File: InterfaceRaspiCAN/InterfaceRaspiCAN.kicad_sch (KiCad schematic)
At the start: 30 parts, among them J1 Raspberry_Pi_2_3, J10 Conn_02x01, J11 Conn_02x01, J12 Conn_02x01, J13 Conn_01x02, J14 Conn_01x02, J15 Conn_01x02, J16 Conn_01x02, J2 CAN1, J3 CAN2, J4 I2C1_5, J5 I2C2_5, U1 MCP2517FD-xSL, U2 MCP2558FD-xSN, U3 PCF8574A, U4 PESD1CAN, Y2 40MHz

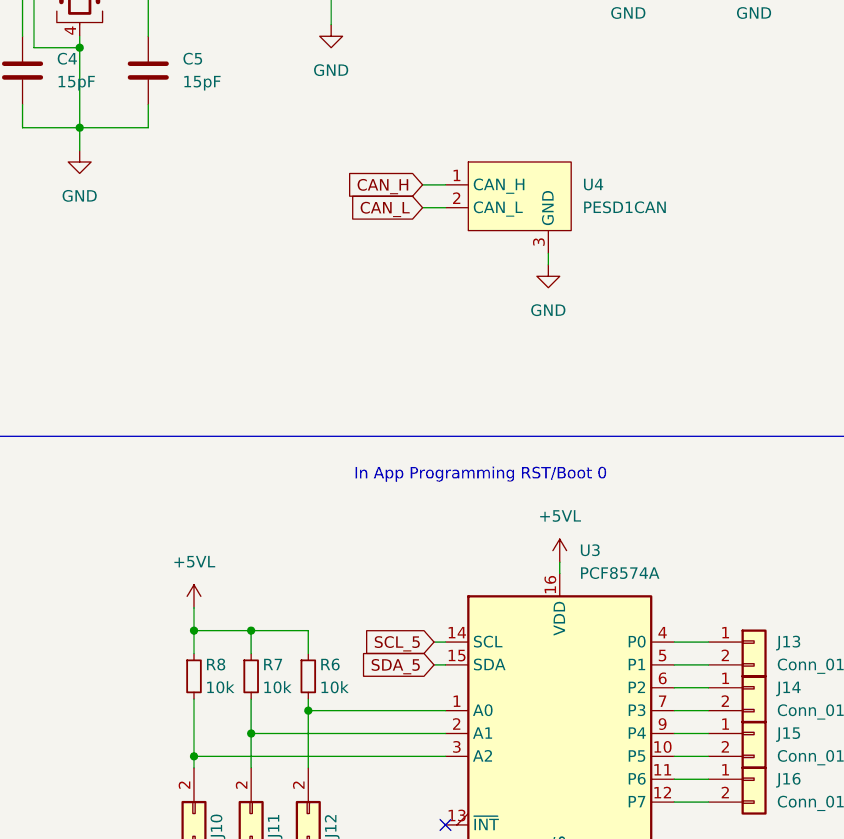
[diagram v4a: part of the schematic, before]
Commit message: In app programming on 3.3V
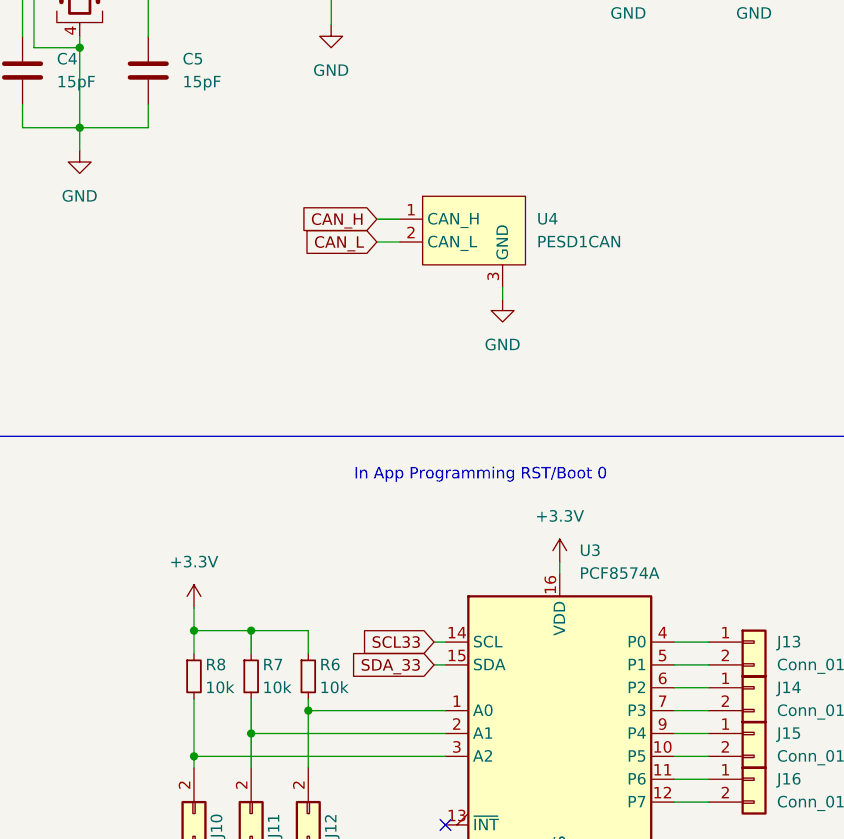
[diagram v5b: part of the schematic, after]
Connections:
- net +3.3V: now also R6.1, R7.1, R8.1, U3.16 (VDD)
- net +5VL: no longer R6.1, R7.1, R8.1, U3.16 (VDD)
- net SCL33: now also U3.14 (SCL)
- net SCL_5: no longer U3.14 (SCL)
- net SDA_33: now also U3.15 (SDA)
- net SDA_5: no longer U3.15 (SDA)
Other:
- moved on the sheet: U4
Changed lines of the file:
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@@
     (stroke (width 0) (type default))
   )
-  (wire (pts (xy 152.4 76.2) (xy 154.94 76.2))
+  (wire (pts (xy 147.32 80.01) (xy 149.86 80.01))
     (stroke (width 0) (type default))
   )
@@
     (stroke (width 0) (type default))
   )
-  (wire (pts (xy 166.37 83.82) (xy 166.37 85.09))
+  (wire (pts (xy 161.29 87.63) (xy 161.29 88.9))
     (stroke (width 0) (type default))
   )
@@
     (stroke (width 0) (type default))
   )
-  (wire (pts (xy 152.4 78.74) (xy 154.94 78.74))
+  (wire (pts (xy 147.32 82.55) (xy 149.86 82.55))
     (stroke (width 0) (type default))
   )
@@
     )
   )
-  (global_label "CAN_L" (shape input) (at 152.4 78.74 180) (fields_autoplaced)
-    (effects (font (size 1.27 1.27)) (justify right))
-    (property "Intersheetrefs" "${INTERSHEET_REFS}" (at 143.73 78.74 0)
+  (global_label "SCL33" (shape input) (at 153.67 127 180) (fields_autoplaced)
+    (effects (font (size 1.27 1.27)) (justify right))
+    (property "Intersheetrefs" "${INTERSHEET_REFS}" (at 144.7582 127 0)
+      (effects (font (size 1.27 1.27)) (justify right) hide)
+    )
+  )
+  (global_label "CAN_L" (shape input) (at 147.32 82.55 180) (fields_autoplaced)
+    (effects (font (size 1.27 1.27)) (justify right))
+    (property "Intersheetrefs" "${INTERSHEET_REFS}" (at 138.65 82.55 0)
       (effects (font (size 1.27 1.27)) (justify right) hide)
     )
@@
     )
   )
-  (global_label "SCL_5" (shape input) (at 153.67 127 180) (fields_autoplaced)
-    (effects (font (size 1.27 1.27)) (justify right))
-    (property "Intersheetrefs" "${INTERSHEET_REFS}" (at 145.0001 127 0)
-      (effects (font (size 1.27 1.27)) (justify right) hide)
-    )
-  )
   (global_label "SPI_MISO" (shape input) (at 80.01 114.3 0) (fields_autoplaced)
     (effects (font (size 1.27 1.27)) (justify left))
@@
     )
   )
-  (global_label "CAN_H" (shape input) (at 152.4 76.2 180) (fields_autoplaced)
-    (effects (font (size 1.27 1.27)) (justify right))
-    (property "Intersheetrefs" "${INTERSHEET_REFS}" (at 143.4276 76.2 0)
+  (global_label "CAN_H" (shape input) (at 147.32 80.01 180) (fields_autoplaced)
+    (effects (font (size 1.27 1.27)) (justify right))
+    (property "Intersheetrefs" "${INTERSHEET_REFS}" (at 138.3476 80.01 0)
       (effects (font (size 1.27 1.27)) (justify right) hide)
     )
@@
     (effects (font (size 1.27 1.27)) (justify right))
     (property "Intersheetrefs" "${INTERSHEET_REFS}" (at 169.7953 36.83 0)
+      (effects (font (size 1.27 1.27)) (justify right) hide)
+    )
+  )
+  (global_label "SDA_33" (shape input) (at 153.67 129.54 180) (fields_autoplaced)
+    (effects (font (size 1.27 1.27)) (justify right))
+    (property "Intersheetrefs" "${INTERSHEET_REFS}" (at 143.7301 129.54 0)
       (effects (font (size 1.27 1.27)) (justify right) hide)
     )
@@
     )
   )
-  (global_label "SDA_5" (shape input) (at 153.67 129.54 180) (fields_autoplaced)
-    (effects (font (size 1.27 1.27)) (justify right))
-    (property "Intersheetrefs" "${INTERSHEET_REFS}" (at 144.9396 129.54 0)
-      (effects (font (size 1.27 1.27)) (justify right) hide)
-    )
-  )
   (global_label "TX" (shape input) (at 175.26 34.29 180) (fields_autoplaced)
     (effects (font (size 1.27 1.27)) (justify right))
@@
     )
   )
-  (symbol (lib_id "ARIG:PESD1CAN") (at 157.48 73.66 0) (unit 1)
-    (in_bom yes) (on_board yes) (dnp no) (fields_autoplaced)
-    (property "Reference" "U4" (at 170.18 76.2 0)
-      (effects (font (size 1.27 1.27)) (justify left))
-    )
-    (property "Value" "PESD1CAN" (at 170.18 78.74 0)
-      (effects (font (size 1.27 1.27)) (justify left))
-    )
-    (property "Footprint" "Package_TO_SOT_SMD:SOT-23" (at 184.15 80.01 0)
-      (effects (font (size 1.27 1.27)) hide)
-    )
-    (property "Datasheet" "https://assets.nexperia.com/documents/data-sheet/PESD1CAN.pdf" (at 203.2 76.2 0)
+  (symbol (lib_id "ARIG:PESD1CAN") (at 152.4 77.47 0) (unit 1)
+    (in_bom yes) (on_board yes) (dnp no) (fields_autoplaced)
+    (property "Reference" "U4" (at 165.1 80.01 0)
+      (effects (font (size 1.27 1.27)) (justify left))
+    )
+    (property "Value" "PESD1CAN" (at 165.1 82.55 0)
+      (effects (font (size 1.27 1.27)) (justify left))
+    )
+    (property "Footprint" "Package_TO_SOT_SMD:SOT-23" (at 179.07 83.82 0)
+      (effects (font (size 1.27 1.27)) hide)
+    )
+    (property "Datasheet" "https://assets.nexperia.com/documents/data-sheet/PESD1CAN.pdf" (at 198.12 80.01 0)
       (effects (font (size 1.27 1.27)) hide)
     )
@@
     )
   )
-  (symbol (lib_id "power:+5VL") (at 167.64 118.11 0) (unit 1)
-    (in_bom yes) (on_board yes) (dnp no) (fields_autoplaced)
-    (property "Reference" "#PWR024" (at 167.64 121.92 0)
-      (effects (font (size 1.27 1.27)) hide)
-    )
-    (property "Value" "+5VL" (at 167.64 113.03 0)
-      (effects (font (size 1.27 1.27)))
-    )
-    (property "Footprint" "" (at 167.64 118.11 0)
-      (effects (font (size 1.27 1.27)) hide)
-    )
-    (property "Datasheet" "" (at 167.64 118.11 0)
+  (symbol (lib_id "power:+3.3V") (at 127 123.19 0) (unit 1)
+    (in_bom yes) (on_board yes) (dnp no) (fields_autoplaced)
+    (property "Reference" "#PWR024" (at 127 127 0)
+      (effects (font (size 1.27 1.27)) hide)
+    )
+    (property "Value" "+3.3V" (at 127 118.11 0)
+      (effects (font (size 1.27 1.27)))
+    )
+    (property "Footprint" "" (at 127 123.19 0)
+      (effects (font (size 1.27 1.27)) hide)
+    )
+    (property "Datasheet" "" (at 127 123.19 0)
       (effects (font (size 1.27 1.27)) hide)
     )
@@
     )
   )
+  (symbol (lib_id "power:+3.3V") (at 167.64 118.11 0) (unit 1)
+    (in_bom yes) (on_board yes) (dnp no) (fields_autoplaced)
+    (property "Reference" "#PWR025" (at 167.64 121.92 0)
+      (effects (font (size 1.27 1.27)) hide)
+    )
+    (property "Value" "+3.3V" (at 167.64 113.03 0)
+      (effects (font (size 1.27 1.27)))
+    )
+    (property "Footprint" "" (at 167.64 118.11 0)
+      (effects (font (size 1.27 1.27)) hide)
+    )
+    (property "Datasheet" "" (at 167.64 118.11 0)
+      (effects (font (size 1.27 1.27)) hide)
+    )
+    (pin "1")
+    (instances
+      (project "InterfaceRaspiCAN"
+        (path "/466ed181-1b10-43ca-b8d2-18d3e4c6e8d6"
+          (reference "#PWR025") (unit 1)
+        )
+      )
+    )
+  )
   (symbol (lib_id "Device:C") (at 83.82 31.75 0) (unit 1)
     (in_bom yes) (on_board yes) (dnp no)
@@
         (path "/466ed181-1b10-43ca-b8d2-18d3e4c6e8d6"
           (reference "J2") (unit 1)
-        )
-      )
-    )
-  )
-  (symbol (lib_id "power:+5VL") (at 127 123.19 0) (unit 1)
-    (in_bom yes) (on_board yes) (dnp no) (fields_autoplaced)
-    (property "Reference" "#PWR029" (at 127 127 0)
-      (effects (font (size 1.27 1.27)) hide)
-    )
-    (property "Value" "+5VL" (at 127 118.11 0)
-      (effects (font (size 1.27 1.27)))
-    )
-    (property "Footprint" "" (at 127 123.19 0)
-      (effects (font (size 1.27 1.27)) hide)
-    )
-    (property "Datasheet" "" (at 127 123.19 0)
-      (effects (font (size 1.27 1.27)) hide)
-    )
-    (pin "1")
-    (instances
-      (project "InterfaceRaspiCAN"
-        (path "/466ed181-1b10-43ca-b8d2-18d3e4c6e8d6"
-          (reference "#PWR029") (unit 1)
         )
       )
@@
     )
   )
-  (symbol (lib_id "power:GND") (at 166.37 85.09 0) (unit 1)
-    (in_bom yes) (on_board yes) (dnp no) (fields_autoplaced)
-    (property "Reference" "#PWR030" (at 166.37 91.44 0)
-      (effects (font (size 1.27 1.27)) hide)
-    )
-    (property "Value" "GND" (at 166.37 90.17 0)
-      (effects (font (size 1.27 1.27)))
-    )
-    (property "Footprint" "" (at 166.37 85.09 0)
-      (effects (font (size 1.27 1.27)) hide)
-    )
-    (property "Datasheet" "" (at 166.37 85.09 0)
-      (effects (font (size 1.27 1.27)) hide)
-    )
+  (symbol (lib_id "power:GND") (at 161.29 88.9 0) (unit 1)
+    (in_bom yes) (on_board yes) (dnp no) (fields_autoplaced)
+    (property "Reference" "#PWR030" (at 161.29 95.25 0)
+      (effects (font (size 1.27 1.27)) hide)
+    )
+    (property "Value" "GND" (at 161.29 93.98 0)
+      (effects (font (size 1.27 1.27)))
+    )
+    (property "Footprint" "" (at 161.29 88.9 0)
+      (effects (font (size 1.27 1.27)) hide)
+    )
+    (property "Datasheet" "" (at 161.29 88.9 0)
+      (effects (font (size 1.27 1.27)) hide)
+    )

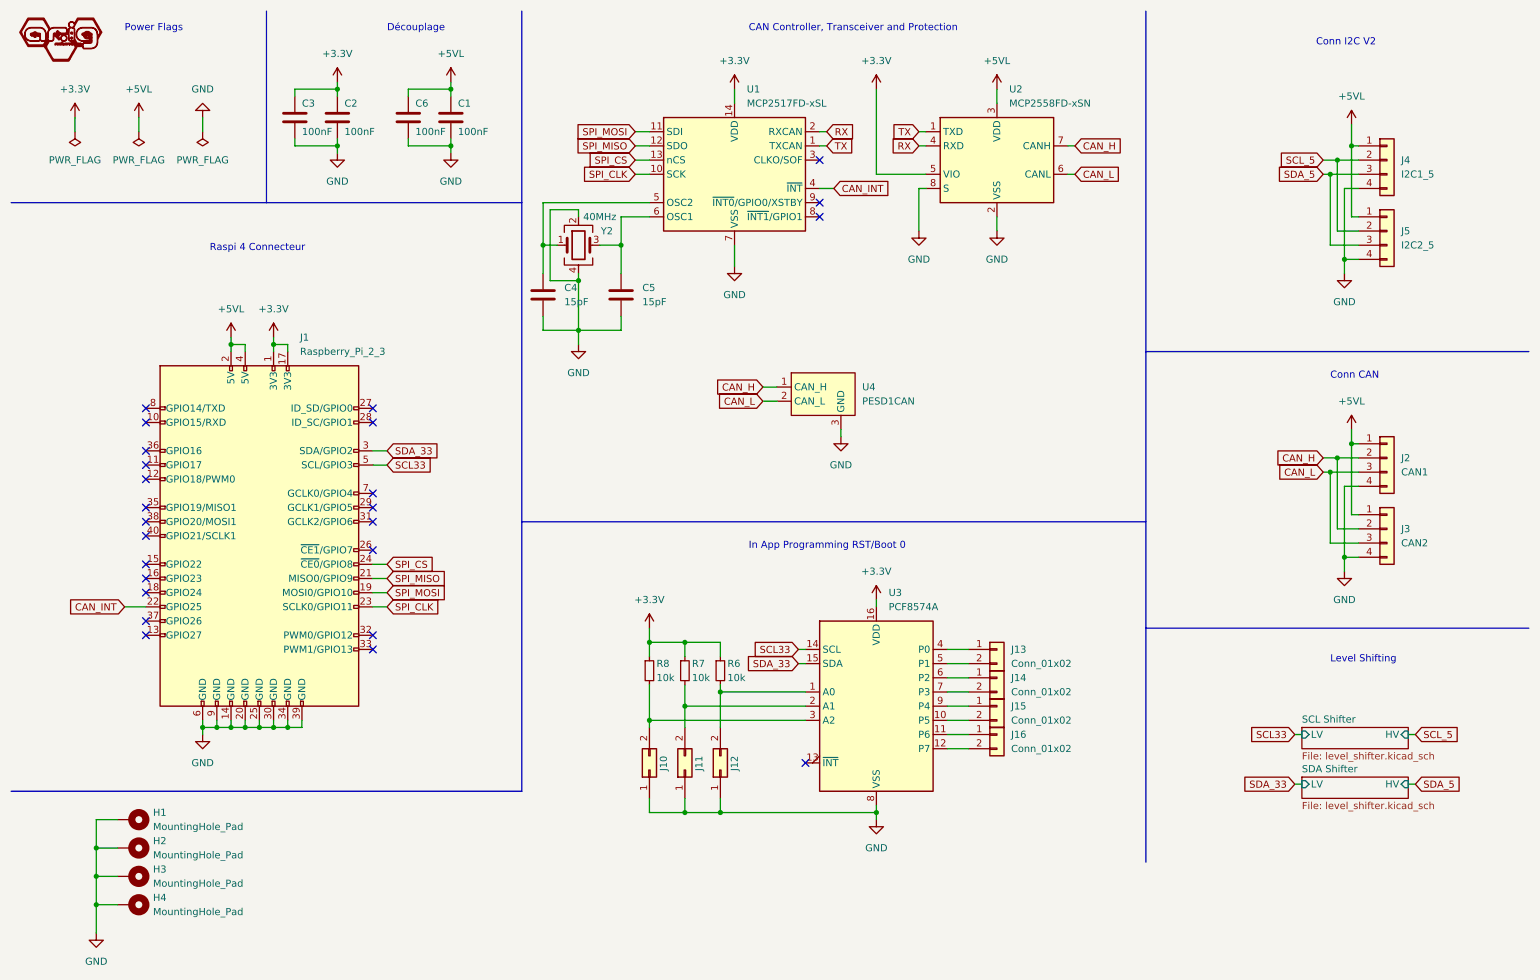
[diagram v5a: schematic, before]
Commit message: Fix CAN connections to improve routing on InterfaceRaspi
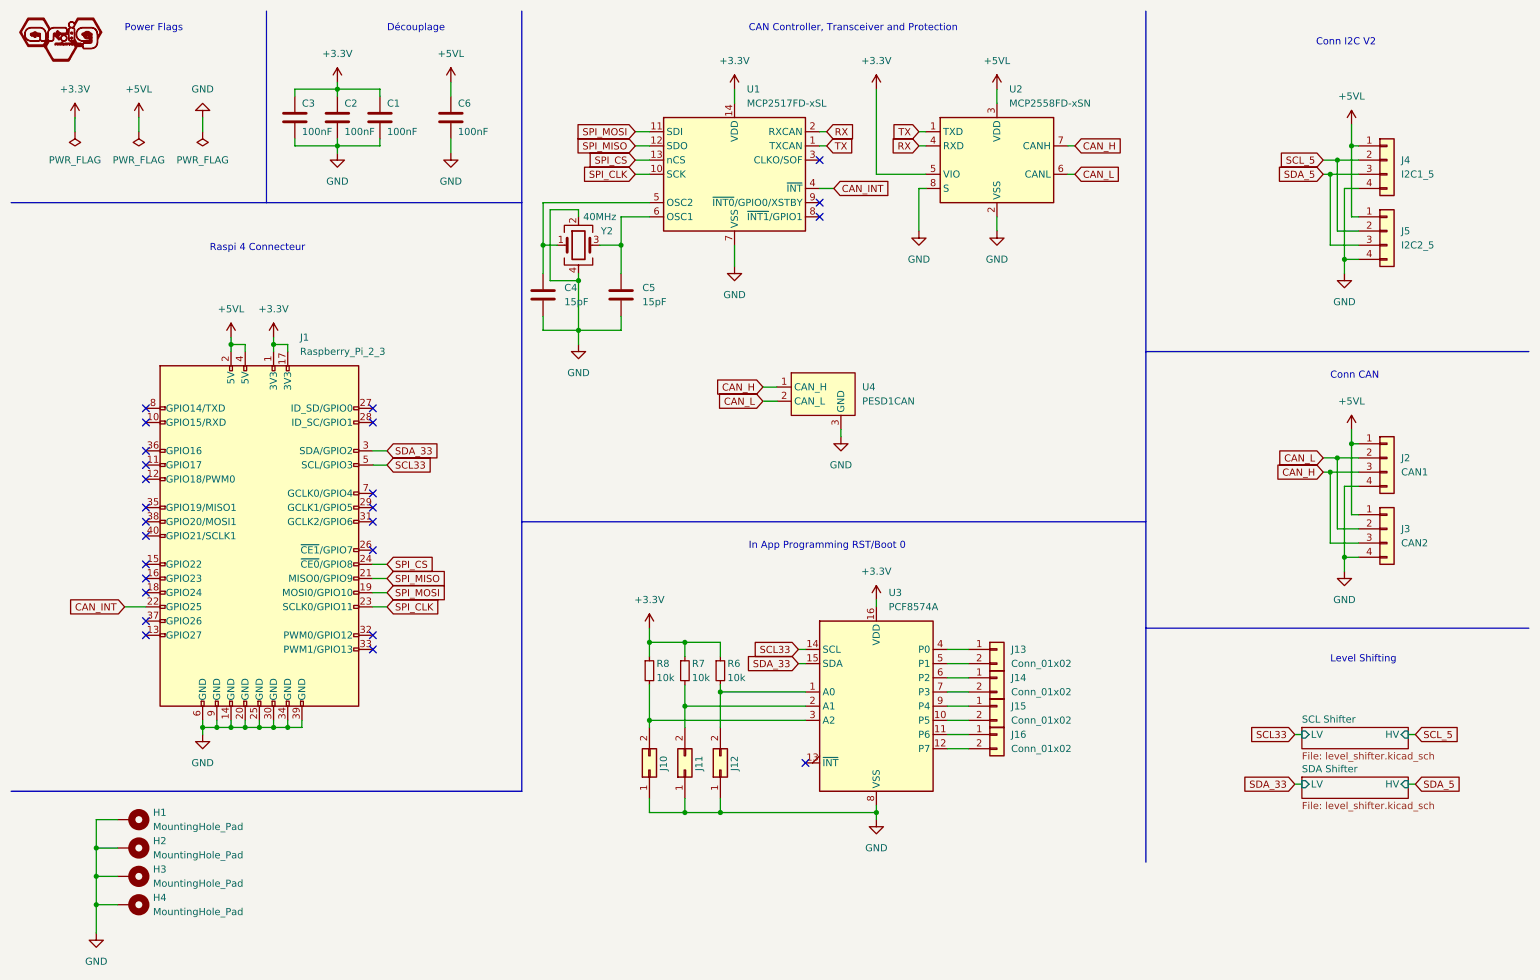
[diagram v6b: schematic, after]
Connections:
- net +3.3V: now also C1.1
- net +5VL: no longer C1.1
- net CAN_H: now also J2.3 (Pin_3), J3.3 (Pin_3); no longer J2.2 (Pin_2), J3.2 (Pin_2)
- net CAN_L: now also J2.2 (Pin_2), J3.2 (Pin_2); no longer J2.3 (Pin_3), J3.3 (Pin_3)
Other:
- moved on the sheet: C1, C6
